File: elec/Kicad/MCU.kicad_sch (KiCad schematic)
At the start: 0 parts

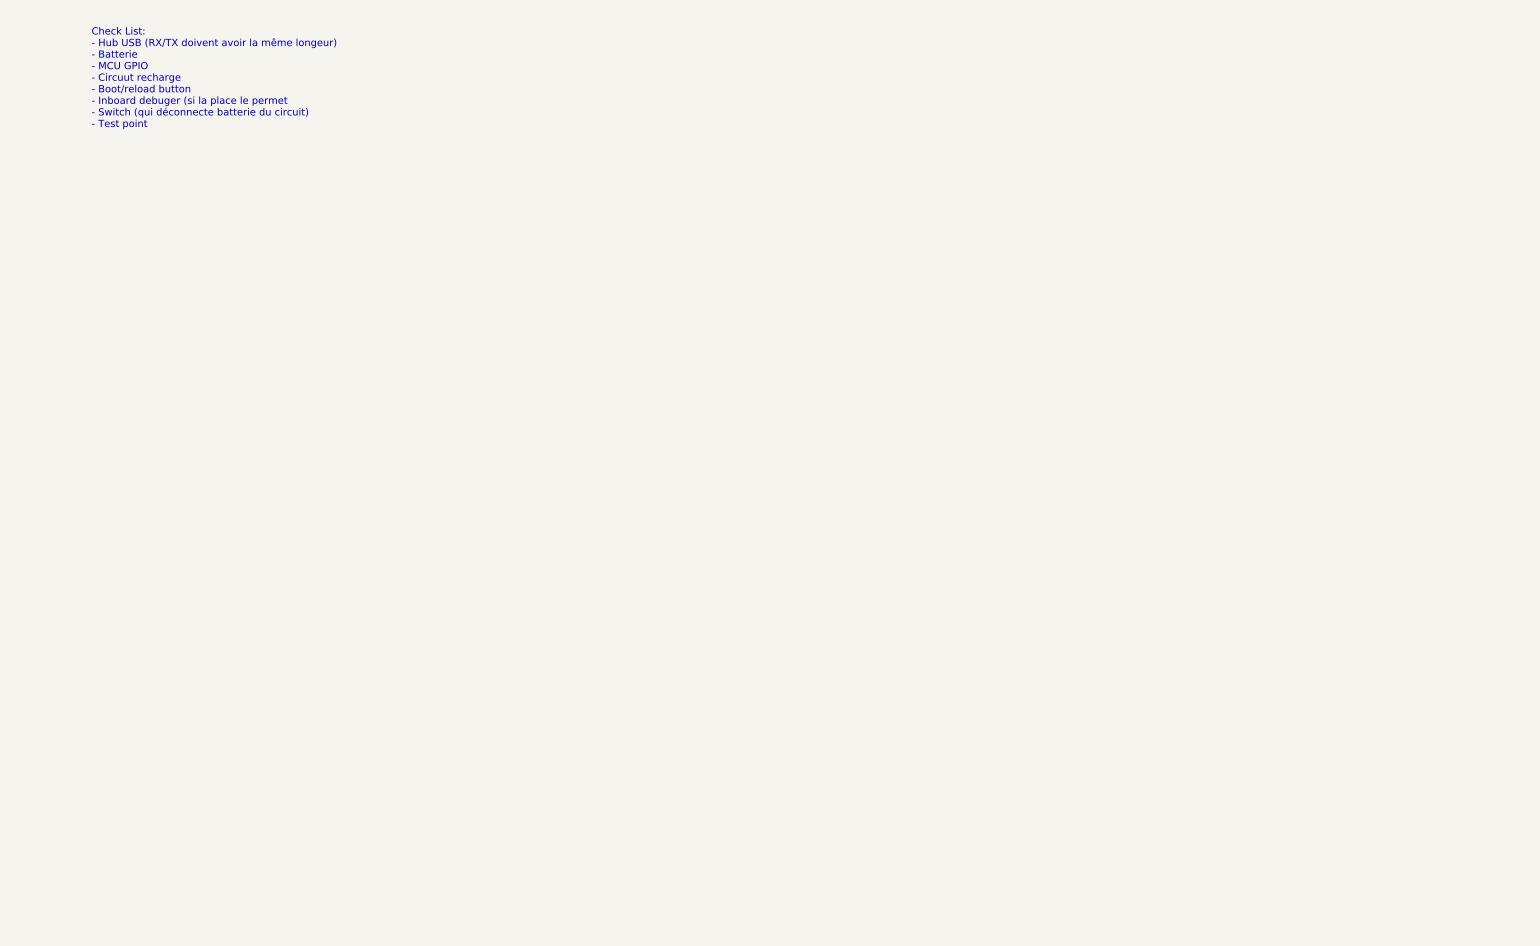
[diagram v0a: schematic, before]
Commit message: add the MCU and embedded deboger footprint in the schematic
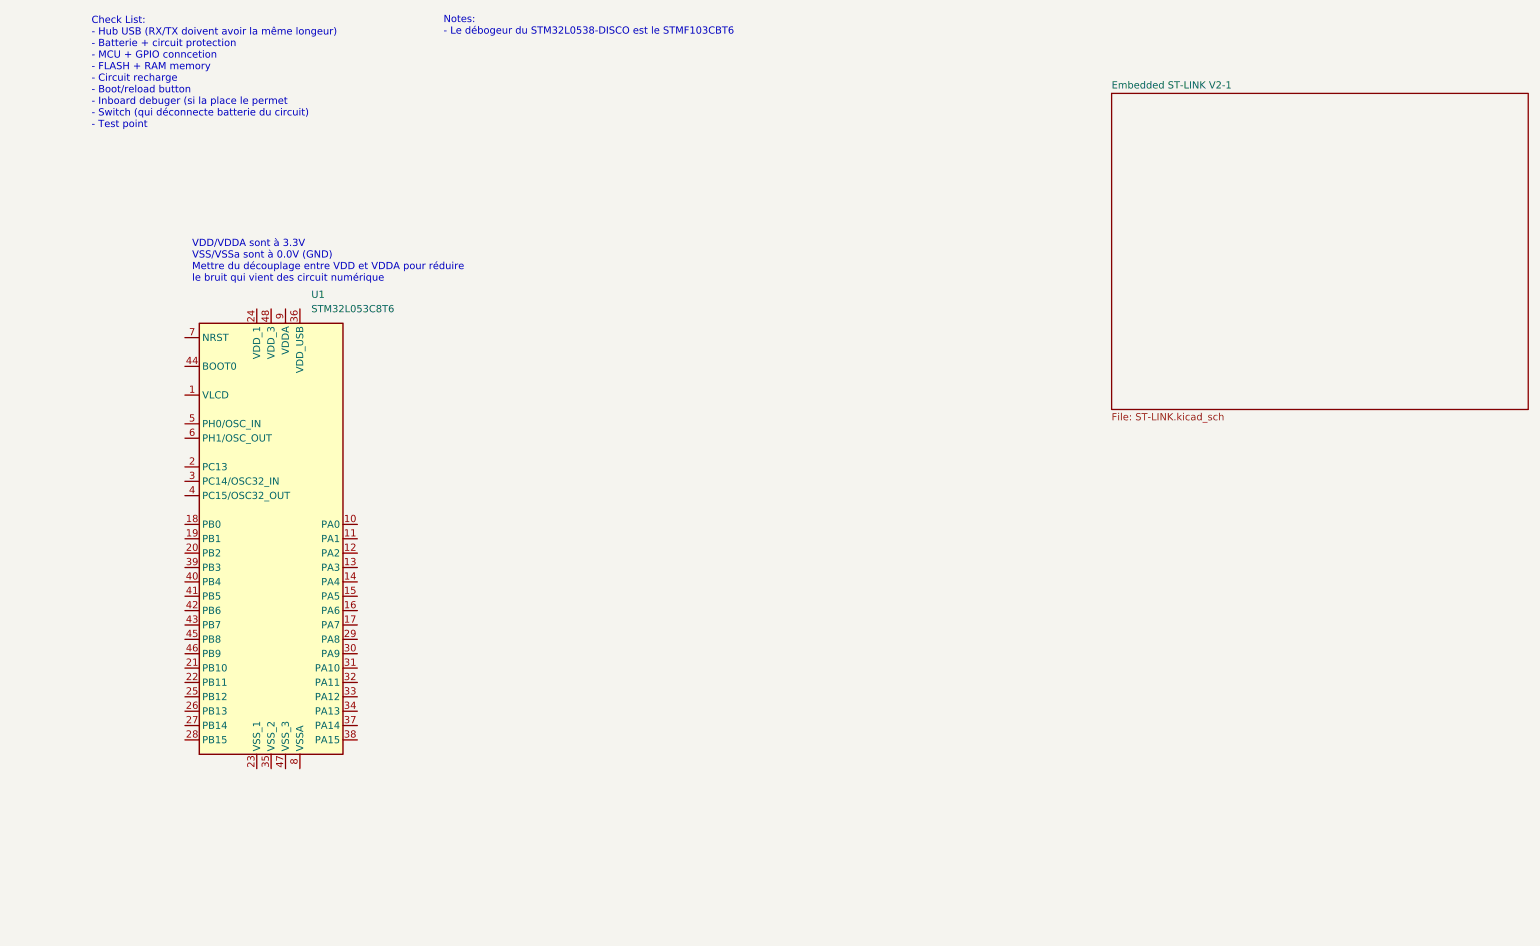
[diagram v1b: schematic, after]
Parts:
- added U1: STM32L053C8T6, Package_QFP:LQFP-48_7x7mm_P0.5mm, symbol MCU_ST_STM32L0:STM32L053C8Tx
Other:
- added sheet Embedded ST-LINK V2-1 (ST-LINK.kicad_sch)
- note added: "Check List: - Hub USB (RX/TX doivent avoir la même longeur) - Batterie + circuit protection - MCU + GPIO conncetion - FLASH + RAM memory - Circuit recharge - Boot/reload button - Inboard debuger (si la place le permet - Switch (qui déconnecte batterie du circuit) - Test point"
- note added: "Notes: - Le débogeur du STM32L0538-DISCO est le STMF103CBT6"
- note added: "VDD/VDDA sont à 3.3V VSS/VSSa sont à 0.0V (GND) Mettre du découplage entre VDD et VDDA pour réduire le bruit qui vient des circuit numérique"
- note removed: "Check List: - Hub USB (RX/TX doivent avoir la même longeur) - Batterie - MCU GPIO - Circuut recharge - Boot/reload button - Inboard debuger (si la place le permet - Switch (qui déconnecte batterie du circuit) - Test point"
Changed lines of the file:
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@@
 (kicad_sch (version 20211123) (generator eeschema)
   (paper "A4")
-  (text "Check List:\n- Hub USB (RX/TX doivent avoir la même longeur)\n- Batterie\n- MCU GPIO\n- Circuut recharge\n- Boot/reload button\n- Inboard debuger (si la place le permet\n- Switch (qui déconnecte batterie du circuit)\n- Test point"
+  (text "Notes:\n- Le débogeur du STM32L0538-DISCO est le STMF103CBT6"
+    (at 83.82 17.78 0)
+    (effects (font (size 1.27 1.27)) (justify left bottom))
+  )
+  (text "Check List:\n- Hub USB (RX/TX doivent avoir la même longeur)\n- Batterie + circuit protection\n- MCU + GPIO conncetion\n- FLASH + RAM memory\n- Circuit recharge\n- Boot/reload button\n- Inboard debuger (si la place le permet\n- Switch (qui déconnecte batterie du circuit)\n- Test point"
     (at 21.59 34.29 0)
     (effects (font (size 1.27 1.27)) (justify left bottom))
   )
+  (text "VDD/VDDA sont à 3.3V\nVSS/VSSa sont à 0.0V (GND)\nMettre du découplage entre VDD et VDDA pour réduire \nle bruit qui vient des circuit numérique\n\n"
+    (at 39.37 63.5 0)
+    (effects (font (size 1.27 1.27)) (justify left bottom))
+  )
+  (symbol (lib_id "MCU_ST_STM32L0:STM32L053C8Tx") (at 53.34 106.68 0) (unit 1)
+    (in_bom yes) (on_board yes) (fields_autoplaced)
+    (property "Reference" "U1" (id 0) (at 60.4394 63.5 0)
+      (effects (font (size 1.27 1.27)) (justify left))
+    )
+    (property "Value" "STM32L053C8T6" (id 1) (at 60.4394 66.04 0)
+      (effects (font (size 1.27 1.27)) (justify left))
+    )
+    (property "Footprint" "Package_QFP:LQFP-48_7x7mm_P0.5mm" (id 2) (at 40.64 144.78 0)
+      (effects (font (size 1.27 1.27)) (justify right) hide)
+    )
+    (property "Datasheet" "http://www.st.com/st-web-ui/static/active/en/resource/technical/document/datasheet/DM00105960.pdf" (id 3) (at 53.34 106.68 0)
+      (effects (font (size 1.27 1.27)) hide)
+    )
+    (pin "1")
+    (pin "10")
+    (pin "11")
+    (pin "12")
+    (pin "13")
+    (pin "14")
+    (pin "15")
+    (pin "16")
+    (pin "17")
+    (pin "18")
+    (pin "19")
+    (pin "2")
+    (pin "20")
+    (pin "21")
+    (pin "22")
+    (pin "23")
+    (pin "24")
+    (pin "25")
+    (pin "26")
+    (pin "27")
+    (pin "28")
+    (pin "29")
+    (pin "3")
+    (pin "30")
+    (pin "31")
+    (pin "32")
+    (pin "33")
+    (pin "34")
+    (pin "35")
+    (pin "36")
+    (pin "37")
+    (pin "38")
+    (pin "39")
+    (pin "4")
+    (pin "40")
+    (pin "41")
+    (pin "42")
+    (pin "43")
+    (pin "44")
+    (pin "45")
+    (pin "46")
+    (pin "47")
+    (pin "48")
+    (pin "5")
+    (pin "6")
+    (pin "7")
+    (pin "8")
+    (pin "9")
+  )
+  (sheet (at 201.93 27.94) (size 73.66 55.88) (fields_autoplaced)
+    (stroke (width 0.1524) (type solid) (color 0 0 0 0))
+    (fill (color 0 0 0 0.0000))
+    (property "Sheet name" "Embedded ST-LINK V2-1" (id 0) (at 201.93 27.2284 0)
+      (effects (font (size 1.27 1.27)) (justify left bottom))
+    )
+    (property "Sheet file" "ST-LINK.kicad_sch" (id 1) (at 201.93 84.4046 0)
+      (effects (font (size 1.27 1.27)) (justify left top))
+    )
+  )
 )

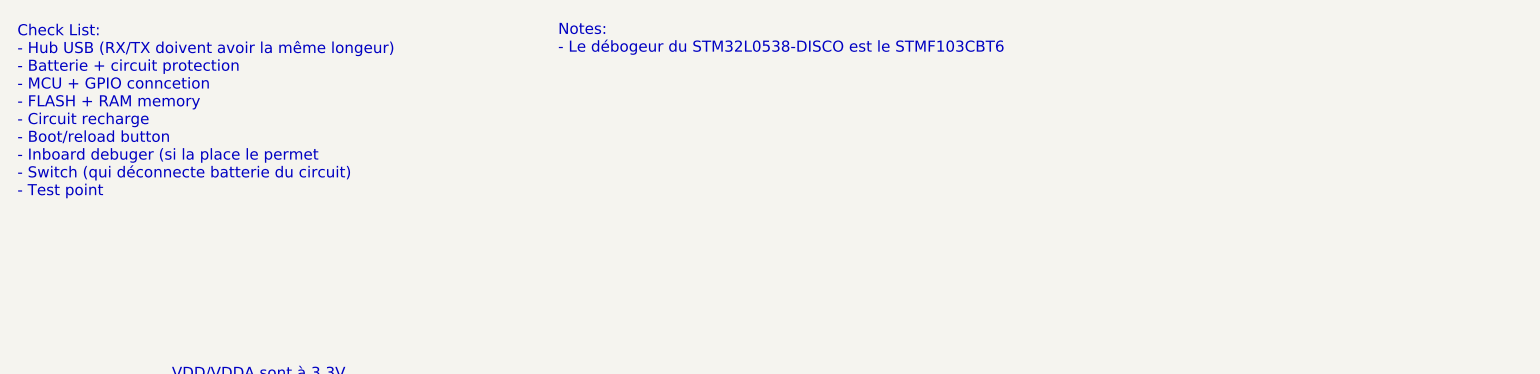
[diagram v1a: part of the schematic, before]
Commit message: add the MCU and embedded debuger footprint in the schematic
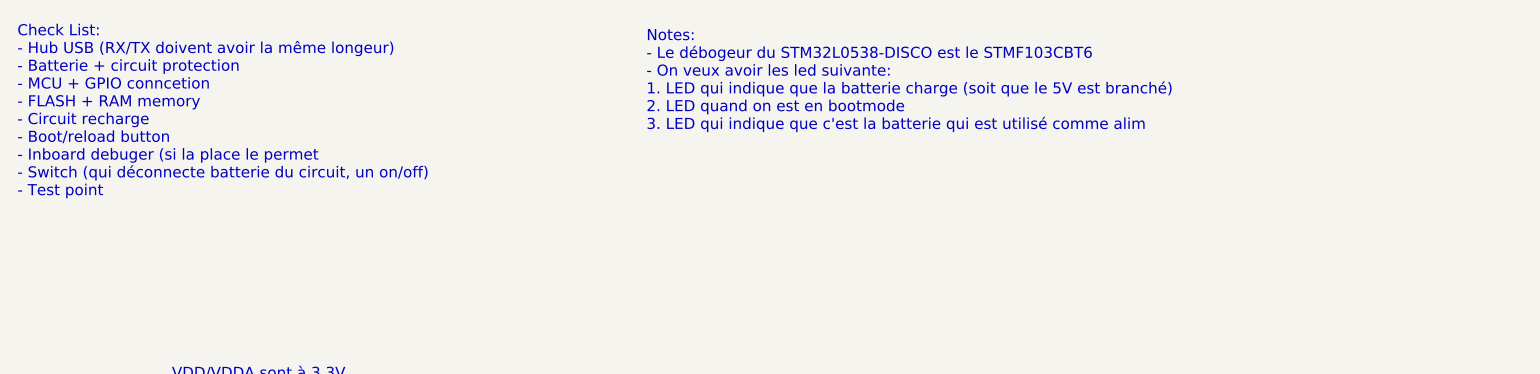
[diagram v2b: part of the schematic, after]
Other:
- note added: "Check List: - Hub USB (RX/TX doivent avoir la même longeur) - Batterie + circuit protection - MCU + GPIO conncetion - FLASH + RAM memory - Circuit recharge - Boot/reload button - Inboard debuger (si la place le permet - Switch (qui déconnecte batterie du circuit, un on/off) - Test point"
- note added: "Notes: - Le débogeur du STM32L0538-DISCO est le STMF103CBT6 - On veux avoir les led suivante: 1. LED qui indique que la batterie charge (soit que le 5V est branché) 2. LED quand on est en bootmode 3. LED qui indique que c'est la batterie qui est utilisé comme alim"
- note removed: "Check List: - Hub USB (RX/TX doivent avoir la même longeur) - Batterie + circuit protection - MCU + GPIO conncetion - FLASH + RAM memory - Circuit recharge - Boot/reload button - Inboard debuger (si la place le permet - Switch (qui déconnecte batterie du circuit) - Test point"
- note removed: "Notes: - Le débogeur du STM32L0538-DISCO est le STMF103CBT6"
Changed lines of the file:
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@@
 (kicad_sch (version 20211123) (generator eeschema)
   (paper "A4")
-  (text "Notes:\n- Le débogeur du STM32L0538-DISCO est le STMF103CBT6"
-    (at 83.82 17.78 0)
+  (text "Notes:\n- Le débogeur du STM32L0538-DISCO est le STMF103CBT6\n- On veux avoir les led suivante: \n1. LED qui indique que la batterie charge (soit que le 5V est branché)\n2. LED quand on est en bootmode\n3. LED qui indique que c'est la batterie qui est utilisé comme alim"
+    (at 93.98 26.67 0)
     (effects (font (size 1.27 1.27)) (justify left bottom))
   )
-  (text "Check List:\n- Hub USB (RX/TX doivent avoir la même longeur)\n- Batterie + circuit protection\n- MCU + GPIO conncetion\n- FLASH + RAM memory\n- Circuit recharge\n- Boot/reload button\n- Inboard debuger (si la place le permet\n- Switch (qui déconnecte batterie du circuit)\n- Test point"
+  (text "Check List:\n- Hub USB (RX/TX doivent avoir la même longeur)\n- Batterie + circuit protection\n- MCU + GPIO conncetion\n- FLASH + RAM memory\n- Circuit recharge\n- Boot/reload button\n- Inboard debuger (si la place le permet\n- Switch (qui déconnecte batterie du circuit, un on/off)\n- Test point"
     (at 21.59 34.29 0)
     (effects (font (size 1.27 1.27)) (justify left bottom))

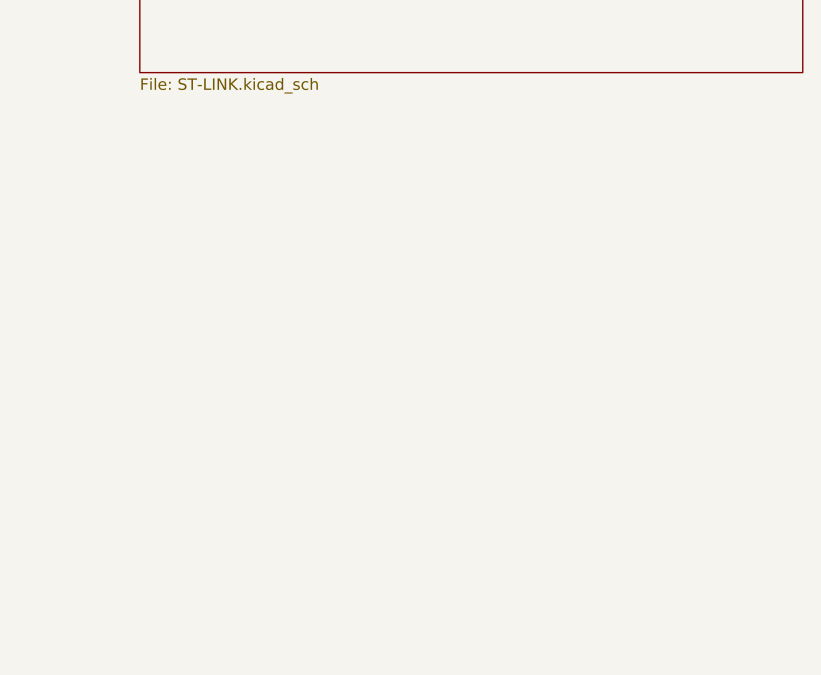
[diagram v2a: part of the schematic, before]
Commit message: add the voltage regulator circuit and the decoupling circuit for VDD/VDDA
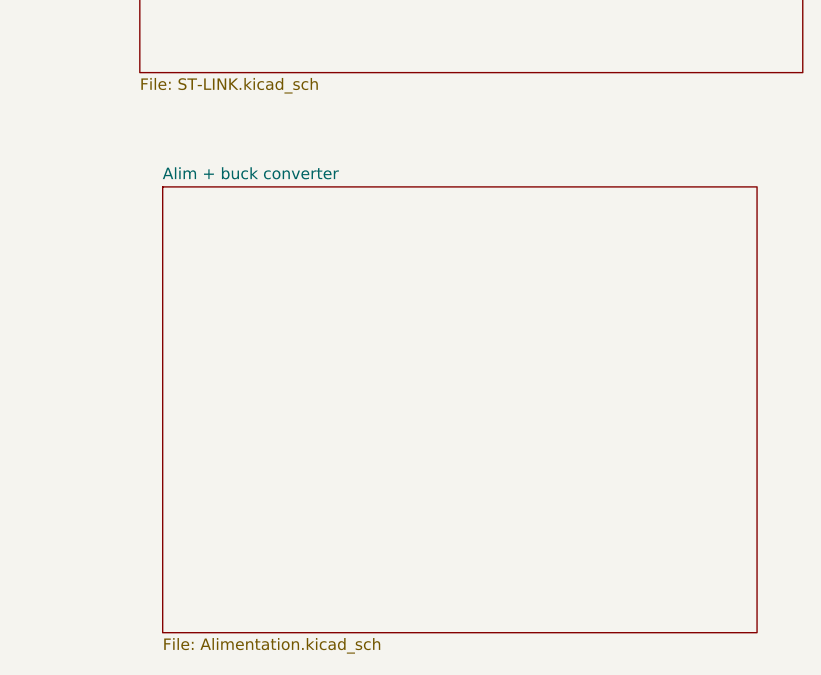
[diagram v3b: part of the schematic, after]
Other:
- added sheet Alim + buck converter (Alimentation.kicad_sch)
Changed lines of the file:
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@@
+    )
+  )
+  (sheet (at 204.47 96.52) (size 66.04 49.53) (fields_autoplaced)
+    (stroke (width 0.1524) (type solid) (color 0 0 0 0))
+    (fill (color 0 0 0 0.0000))
+    (property "Sheet name" "Alim + buck converter" (id 0) (at 204.47 95.8084 0)
+      (effects (font (size 1.27 1.27)) (justify left bottom))
+    )
+    (property "Sheet file" "Alimentation.kicad_sch" (id 1) (at 204.47 146.6346 0)
+      (effects (font (size 1.27 1.27)) (justify left top))
     )
   )

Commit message: did some change (but i have to verify them)
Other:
- note added: "VDD/VDDA sont à 3.3V VSS/VSSA sont à 0.0V (GND) Mettre du découplage entre VDD et VDDA pour réduire le bruit qui vient des circuit numérique"
- note removed: "VDD/VDDA sont à 3.3V VSS/VSSa sont à 0.0V (GND) Mettre du découplage entre VDD et VDDA pour réduire le bruit qui vient des circuit numérique"
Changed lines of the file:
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@@
     (effects (font (size 1.27 1.27)) (justify left bottom))
   )
-  (text "VDD/VDDA sont à 3.3V\nVSS/VSSa sont à 0.0V (GND)\nMettre du découplage entre VDD et VDDA pour réduire \nle bruit qui vient des circuit numérique\n\n"
+  (text "VDD/VDDA sont à 3.3V\nVSS/VSSA sont à 0.0V (GND)\nMettre du découplage entre VDD et VDDA pour réduire \nle bruit qui vient des circuit numérique\n\n"
     (at 39.37 63.5 0)
     (effects (font (size 1.27 1.27)) (justify left bottom))

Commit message: boot/reset button
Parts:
- added C? (x2): 100nF, symbol Device:C
- added R? (x2): 10K, symbol Device:R
- added SW? (x2): SW_Push_RESET, symbol Switch:SW_Push
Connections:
- net +3V3: now reaches U1.24 (VDD_1)
- net +3V3: now also U1.36 (VDD_USB), U1.48 (VDD_3), R?.1, R?.1, SW?.1
- net BOOT0: now reaches U1.44 (BOOT0)
- net BOOT0: now also C?.1, SW?.2
- net NRST: now reaches U1.7 (NRST)
- net NRST: now also C?.1, R?.2, SW?.2
- net +3.3VA: now reaches U1.9 (VDDA)
- new net GND: C?.2, C?.2, R?.2, SW?.1
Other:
- note added: "BOOT0: 1 = Bootloader, 0 = Run"
- moved on the sheet: U1

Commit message: merci Linux
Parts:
- added C2, C3: 22pF, symbol Device:C
- added D2: GREEN, symbol Device:LED
- added R2, R3: 1K5, symbol Device:R
- added Y1: 32MHz, symbol Device:Crystal
- SW?: value SW_Push_RESET -> SW_Push_BOOT
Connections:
- net +3V3: now also R2.1
- net GND: now also U1.23 (VSS_1), U1.35 (VSS_2), U1.47 (VSS_3), U1.8 (VSSA), C2.2, C3.2, R3.2
- net LED_STAT: now reaches U1.11 (PA1)
- net LED_STAT: now also D2.2 (A)
- net USB_D-: now reaches U1.32 (PA11)
- net USB_D+: now reaches U1.33 (PA12)
- net USB_D+: now also R2.2
- net SWDIO: now reaches U1.34 (PA13)
- net SWCLK: now reaches U1.37 (PA14)
- new net: D2.1 (K), R3.1
- new net PH0: C3.1, Y1.1
- new net PH1: C2.1, Y1.2
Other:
- note added: "Bootloader (HIGH) = boot from system memory. Else (LOW) = boot from flash memory"
- note added: "Clock"
- note added: "NEAR MCU"
- note added: "NRST: 1 = normal operation, 0 = reset the system"
- note added: "Quand on appuie, on pull BOOT0 a high"
- moved on the sheet: C?, R?, SW?, U1
